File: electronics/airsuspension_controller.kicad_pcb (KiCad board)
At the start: 2 copper layers, 100 x 100 mm, 113 parts, among them Q1 BSS138, Q2 BC847, U1 ITS5215L, U10 Teensy3.1, U2 BTS6133D, U3 ITS5215L, U4 ITS5215L, U5 ITS5215L, U6 LM224, U7 LM224, U8 SN65HVD1050D, U9 LM2574M-5

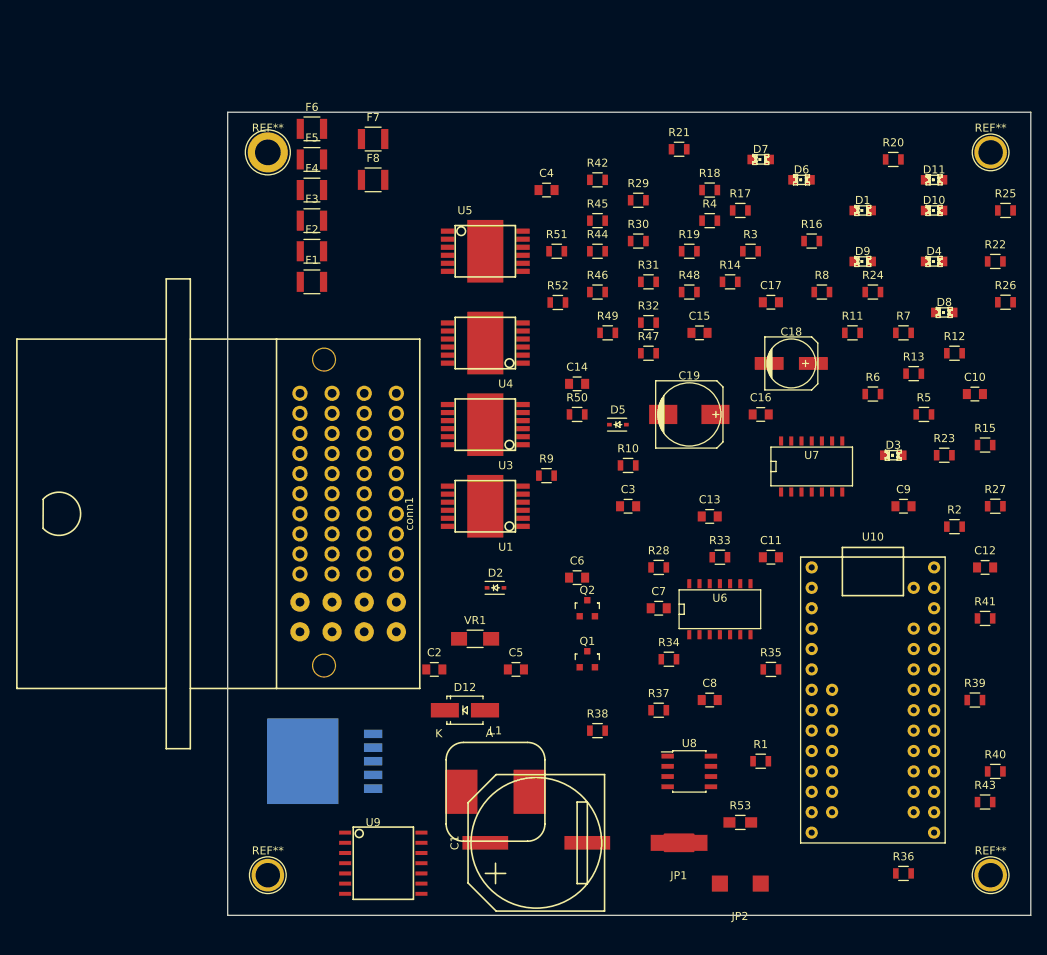
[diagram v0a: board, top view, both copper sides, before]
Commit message: Changed to a more stable powersupply (3Amps 5V and separate 3.3v) + some few cleanups due to updated kicad
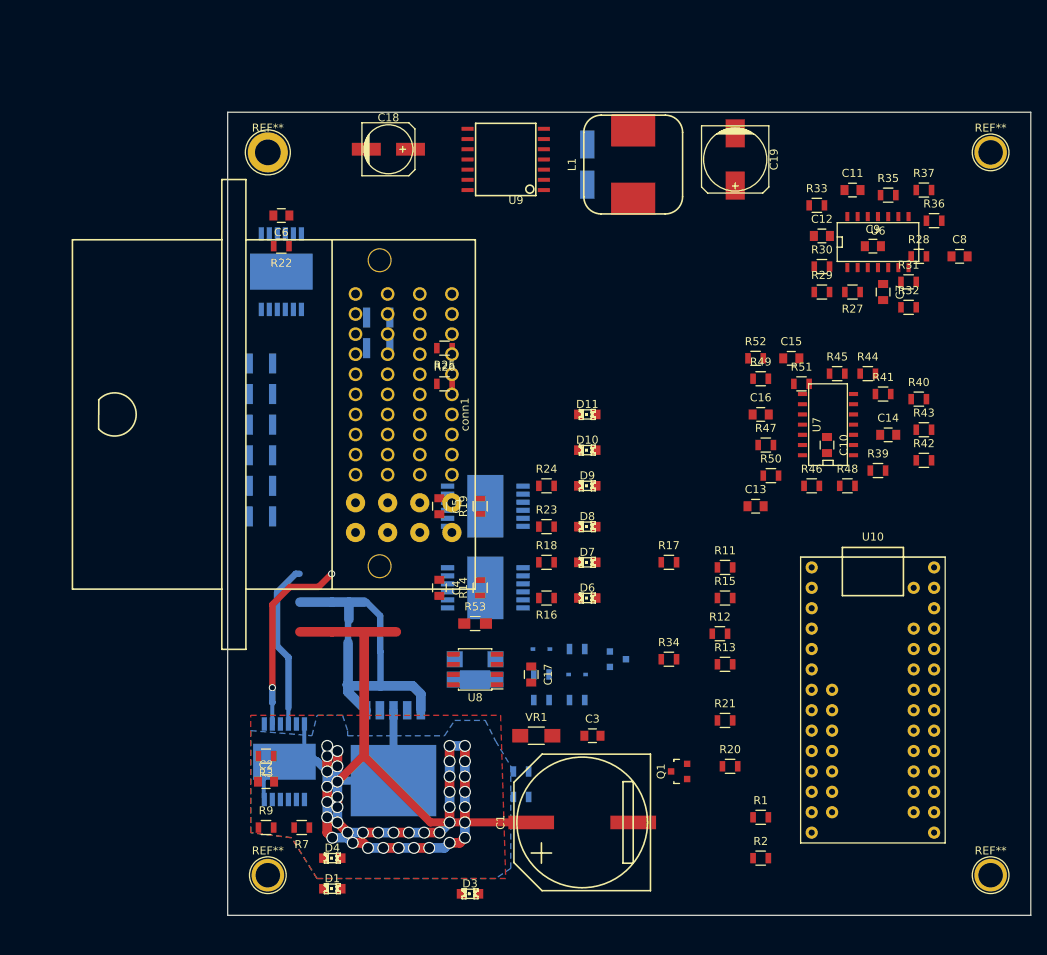
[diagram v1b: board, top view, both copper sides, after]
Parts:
- D12, D2, D5, F1, F2, F3, F4, F5, F6, F7, F8, JP1, JP2, Q2, R10, R38, R4, R5, R6, R8, U1, U3, U4, U5: moved to B.Cu
- moved D1 107.2 mm to (113.0, 146.7)
- moved D4 105.5 mm to (113.0, 142.9)
- moved R7 97.0 mm to (109.2, 139.1), turned to 180 degrees
- moved U9 88.9 mm to (134.6, 55.9), turned to 180 degrees
- moved R22 88.9 mm to (106.7, 66.7), turned to 180 degrees
- moved R3 87.1 mm to (104.8, 130.2), turned to 180 degrees
- moved R36 81.4 mm to (188.0, 63.5)
- moved L1 80.0 mm to (150.5, 56.5), turned to 90 degrees
- moved R20 78.2 mm to (162.6, 131.4)
- moved D3 75.9 mm to (130.2, 147.3)
- moved R37 72.7 mm to (186.7, 59.7)
- moved R4 72.5 mm to (136.5, 132.1)
- moved R25 71.9 mm to (127.0, 79.4), turned to 180 degrees
- moved R21 71.3 mm to (161.9, 125.7)
- moved R26 70.6 mm to (127.0, 83.8)
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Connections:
- C11 pad 2: GND -> Net-(C11-Pad2)
- C12 pad 2: GND -> Net-(C12-Pad2)
- conn1 pad L1: GNDPWR -> /Outputs/Compressor_OUT
- conn1 pad L4: /Outputs/Compressor_OUT -> GNDPWR
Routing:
- net +12V_bat: track 0.00 -> 168.8 mm, vias 0 -> 40
- net /Outputs/Compressor_OUT: track 0.00 -> 46.0 mm
- net /Outputs/RightFill_OUT: track 0.00 -> 23.9 mm, vias 0 -> 2
- net /Outputs/LeftFill_Out: track 0.00 -> 20.8 mm
- added copper zone on B.Cu, net +12V_bat
- added copper zone on F.Cu, net +12V_bat
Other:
- net class power: clearance 0.45 -> 0.376

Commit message: First placement with a ModICE enclosure
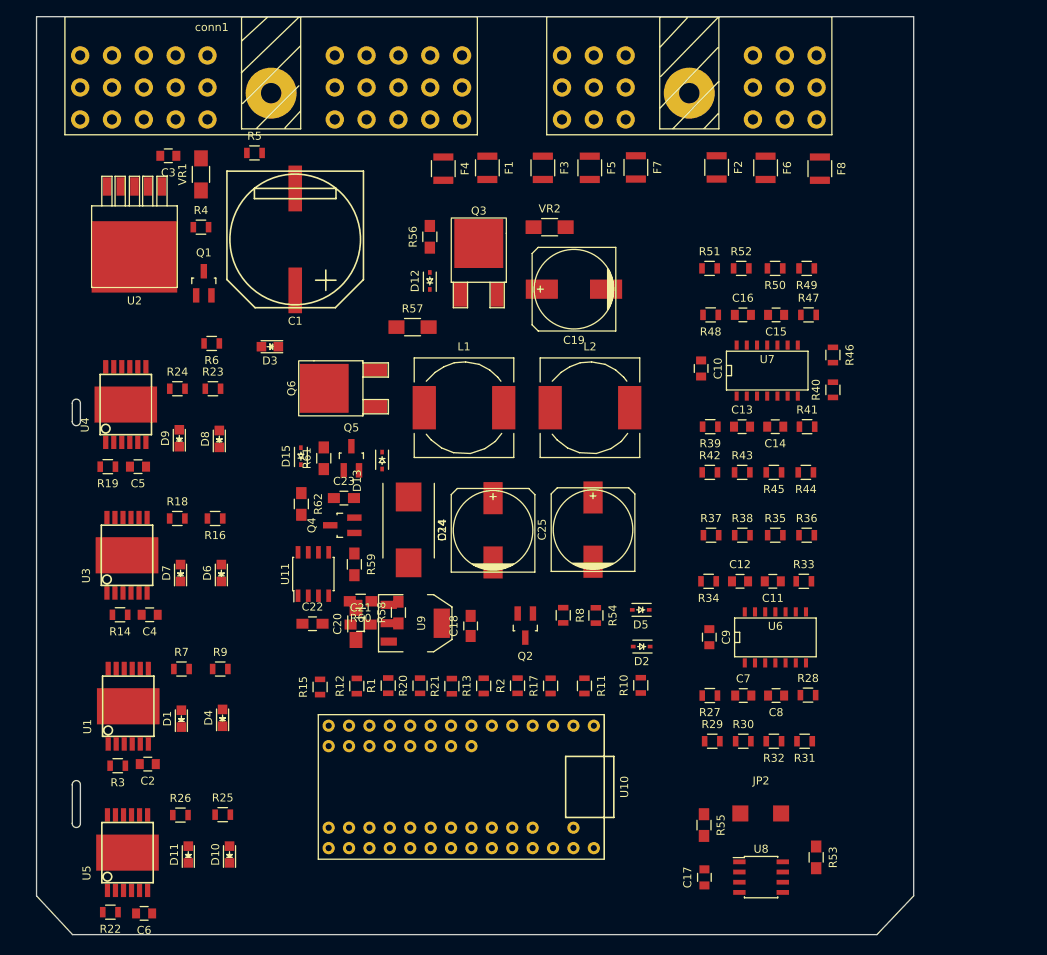
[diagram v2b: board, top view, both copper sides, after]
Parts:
- removed JP1: CAN_fullspeed, Oddities:NetTie-I_Connected_SMD
- removed REF** (x4): 1pin, Connect:1pin
- added C20: 10uF, Capacitors_SMD:C_1206_HandSoldering, F.Cu at (116.0, 113.7)
- added C21: 100n, Capacitors_SMD:C_0805_HandSoldering, F.Cu at (116.6, 113.8)
- added C22: 1n, Capacitors_SMD:C_0805_HandSoldering, F.Cu at (110.6, 113.7)
- added C23: 100n, Capacitors_SMD:C_0805_HandSoldering, F.Cu at (114.5, 98.0)
- added C24: 680uF, Capacitors_SMD:c_elec_10x10.5, F.Cu at (133.0, 102.1)
- added C25: 680uF, Capacitors_SMD:c_elec_10x10.5, F.Cu at (145.5, 102.0)
- added D13: 1n4148w, Diodes_SMD:SOD-323, F.Cu at (119.2, 93.4)
- added D14: schotky, Diodes_SMD:DO-214AB_Handsoldering, F.Cu at (122.5, 102.0)
- added D15: 1n4148w, Diodes_SMD:SOD-323, F.Cu at (109.1, 92.8)
- added L2: SRR1240-180M 17.4uH, Inductors_NEOSID:Neosid_Inductor_SM-NE127, F.Cu at (145.1, 86.8)
- added Q3: IPD50P04P4L-11, TO_SOT_Packages_SMD:TO-252-2Lead, F.Cu at (131.3, 72.7)
- added Q4: BC856, TO_SOT_Packages_SMD:SOT-23_Handsoldering, F.Cu at (114.3, 101.4)
- added Q5: BC856, TO_SOT_Packages_SMD:SOT-23_Handsoldering, F.Cu at (115.4, 93.1)
- added Q6: IPD060N03L G, TO_SOT_Packages_SMD:TO-252-2Lead, F.Cu at (118.4, 84.4)
- added R54: 1k, Resistors_SMD:R_0805, F.Cu at (145.8, 112.7)
- added R55: 10k, Resistors_SMD:R_0805_HandSoldering, F.Cu at (159.3, 138.8)
- added R56: 10k, Resistors_SMD:R_0805_HandSoldering, F.Cu at (125.2, 65.5)
- added R57: 0.031, Resistors_SMD:R_1206_HandSoldering, F.Cu at (123.0, 76.8)
- added R58: 1.2k, Resistors_SMD:R_0805_HandSoldering, F.Cu at (121.3, 112.3)
- added R59: 10k, Resistors_SMD:R_0805_HandSoldering, F.Cu at (115.8, 106.3)
- added R60: 3.6k, Resistors_SMD:R_0805_HandSoldering, F.Cu at (116.6, 110.9)
- added R61: 10k, Resistors_SMD:R_0805_HandSoldering, F.Cu at (112.0, 93.1)
- added R62: 10, Resistors_SMD:R_0805_HandSoldering, F.Cu at (109.2, 98.8)
- added U11: MC34063, Housings_SOIC:SOIC-8_3.9x4.9mm_Pitch1.27mm, F.Cu at (110.7, 107.5)
- added VR2: VR, Resistors_SMD:R_1206_HandSoldering, F.Cu at (140.1, 64.3)
- C18: value 47uF lowESR -> 100nF; footprint Capacitors_SMD:c_elec_6.3x7.7 -> Capacitors_SMD:C_0805_HandSoldering
- C19: value 470uF low esr -> 680uF; footprint Capacitors_SMD:c_elec_8x10.5 -> Capacitors_SMD:c_elec_10x10.5
- D1, D10, D11, D3, D4, D6, D7, D8, D9: footprint LEDs:LED-0805 -> LEDs:LED_0805
- D12: value SS110 -> 10v; footprint Diodes_SMD:Diode-SMA_Handsoldering -> Diodes_SMD:SOD-323; moved to F.Cu
- D2, D5, F1, F2, F3, F4, F5, F6, F7, F8, JP2, R10, R38, R4, R5, R6, U1, U3, U4, U5: moved to F.Cu
- L1: value 470uH -> SRR1240-180M 17.4uH; footprint kicad_lib:Inductor_MSS1260 -> Inductors_NEOSID:Neosid_Inductor_SM-NE127
- Q1: footprint Housings_SOT-23_SOT-143_TSOT-6:SOT-23 -> TO_SOT_Packages_SMD:SOT-23_Handsoldering
- Q2: footprint Housings_SOT-23_SOT-143_TSOT-6:SOT-23 -> TO_SOT_Packages_SMD:SOT-23_Handsoldering; moved to F.Cu
- R8: value 10k -> 1k; moved to F.Cu
- U2: footprint SMD_Packages:DPAK-5 -> kicad_lib:bts6133d; moved to F.Cu
- U9: value LM2574M-5 -> LD1117S33CTR; footprint kicad_lib:SOIC14_W -> TO_SOT_Packages_SMD:SOT-223
- conn1: value conn_molex_36638-48pin -> Conn48pin; footprint kicad_lib:Molex_48way_36638 -> cinch:Conn48pin
- moved C3 89.5 mm to (92.6, 55.4), turned to 180 degrees
- moved C6 88.6 mm to (89.6, 149.8)
- moved R22 85.6 mm to (85.4, 149.6)
- moved Q1 84.8 mm to (97.0, 71.3), turned to 0 degrees
- moved VR1 81.4 mm to (96.7, 57.7), turned to 90 degrees
- moved C1 80.9 mm to (108.4, 65.8), turned to 0 degrees
- moved R4 78.6 mm to (96.7, 64.3)
- moved R5 76.9 mm to (103.3, 55.1)
- moved U5 74.8 mm to (87.5, 142.2), turned to 90 degrees
- moved D11 74.0 mm to (95.1, 142.4), turned to 90 degrees
- moved U2 72.8 mm to (88.4, 59.2), turned to 180 degrees
- moved D3 72.5 mm to (105.3, 79.2), turned to 180 degrees
- moved F2 69.2 mm to (160.9, 56.9), turned to 270 degrees
- moved R6 68.4 mm to (98.0, 78.8)
- moved D10 67.2 mm to (100.2, 142.4), turned to 90 degrees
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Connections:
- net /CAN_bus/CAN_RX renamed /CAN_RX
- net /CAN_bus/CAN_TX renamed /CAN_TX
- net /Inputs/AnalogSpare_3.3V renamed /AnalogSpare_3.3V
- net /Inputs/LeftHeightPot_3.3V renamed /LeftHeight_3.3V
- net /Inputs/LeftPressure_3.3V renamed /LeftPressure_3.3V
- net /Inputs/RightHeightPot_3.3V renamed /RightHeight_3.3V
- net /Inputs/RightPressure_3.3V renamed /RightPressure_3.3V
- net /Inputs/SpareTemp_3.3V renamed /SpareTemp_3.3V
- net /Microcontroller/Airdryer_DIAG renamed /Airdryer_DIAG
- net /Microcontroller/Airdryer_ON renamed /Airdryer_ON
- net /Microcontroller/CompressorTemp_3.3V renamed /CompressorTemp_3.3V
- net /Microcontroller/Compressor_DIAG renamed /Compressor_DIAG
- net /Microcontroller/Compressor_ON renamed /Compressor_ON
- net /Microcontroller/Compressor_Pressure_3.3V renamed /CompressorPressure_3.3V
- net /Microcontroller/LeftDump_DIAG renamed /LeftDump_DIAG
- net /Microcontroller/LeftDump_ON renamed /LeftDump_ON
- net /Microcontroller/LeftFill_DIAG renamed /LeftFill_DIAG
- net /Microcontroller/LeftFill_ON renamed /LeftFill_ON
- net /Microcontroller/LeftSuck_DIAG renamed /LeftSuck_DIAG
- net /Microcontroller/LeftSuck_ON renamed /LeftSuck_ON
- net /Microcontroller/RightDump_DIAG renamed /RightDump_DIAG
- net /Microcontroller/RightDump_ON renamed /RightDump_ON
- net /Microcontroller/RightFill_DIAG renamed /RightFill_DIAG
- net /Microcontroller/RightFill_ON renamed /RightFill_ON
- net /Microcontroller/RightSuck_DIAG renamed /RightSuck_DIAG
- net /Microcontroller/RightSuck_ON renamed /RightSuck_ON
- net /Microcontroller/Spare1_Diag renamed /Spare1_DIAG
- net /Microcontroller/Spare1_ON renamed /Spare1_ON
- C11 pad 2: Net-(C11-Pad2) -> GND
- C12 pad 2: Net-(C12-Pad2) -> GND
- C18 pad 1: /5V power/+12V_IGN -> +5V
- C19 pad 1: +5V -> /5V power/+12V_IGN_SAFE
- D1 pad 1: Net-(D1-Pad1) -> GNDPWR
- D1 pad 2: GNDPWR -> Net-(D1-Pad2)
- D10 pad 1: Net-(D10-Pad1) -> GNDPWR
- D10 pad 2: GNDPWR -> Net-(D10-Pad2)
- D11 pad 1: Net-(D11-Pad1) -> GNDPWR
- D11 pad 2: GNDPWR -> Net-(D11-Pad2)
- D12 pad 1: GND -> /5V power/+12V_IGN_SAFE
- D3 pad 1: Net-(D3-Pad1) -> GNDPWR
- D3 pad 2: GNDPWR -> Net-(D3-Pad2)
- D4 pad 1: Net-(D4-Pad1) -> GNDPWR
- D4 pad 2: GNDPWR -> Net-(D4-Pad2)
- D5 pad 1: GND -> /CompressorCurrent_3.3V
- D5 pad 2: /Microcontroller/Compressor_Current -> GND
- D6 pad 1: Net-(D6-Pad1) -> GNDPWR
- D6 pad 2: GNDPWR -> Net-(D6-Pad2)
- D7 pad 1: Net-(D7-Pad1) -> GNDPWR
- D7 pad 2: GNDPWR -> Net-(D7-Pad2)
- D8 pad 1: Net-(D8-Pad1) -> GNDPWR
- D8 pad 2: GNDPWR -> Net-(D8-Pad2)
- D9 pad 1: Net-(D9-Pad1) -> GNDPWR
- D9 pad 2: GNDPWR -> Net-(D9-Pad2)
- F1 pad 1: /Inputs/CompressorPressure_5V -> /CompressorPressure_5V
- F2 pad 1: /Inputs/RightHeightPot_5V -> /RightHeightPot_5V
- F3 pad 1: /Inputs/LeftPressure_5V -> /LeftPressure_5V
- F4 pad 1: /Inputs/AnalogSpare_5V -> /AnalogSpare_5V
- F5 pad 1: /Inputs/RightPressure_5V -> /RightPressure_5V
- F6 pad 1: /Inputs/CompressorTemp_5V -> /CompressorTemp_5V
- F7 pad 1: /Inputs/LeftHeightPot_5V -> /LeftHeightPot_5V
- F8 pad 1: /Inputs/SpareTemp_5V -> /SpareTemp_5V
- L1 pad 1: Net-(D12-Pad2) -> Net-(C23-Pad2)
- L1 pad 2: +5V -> Net-(C24-Pad1)
- R10 pad 1: /Microcontroller/Compressor_Current -> /CompressorCurrent_3.3V
- R10 pad 2: Net-(D2-Pad2) -> Net-(D2-Pad1)
- R16 pad 1: Net-(D6-Pad1) -> Net-(D6-Pad2)
- R16 pad 2: /Outputs/RightDump_OUT -> /RightDump_OUT
- R18 pad 1: /Outputs/LeftDump_Out -> /LeftDump_OUT
- R18 pad 2: Net-(D7-Pad1) -> Net-(D7-Pad2)
- R23 pad 1: Net-(D8-Pad1) -> Net-(D8-Pad2)
- R23 pad 2: /Outputs/Spare1_OUT -> /Spare1_OUT
- R24 pad 1: /Outputs/Airdryer_Out -> /AirDryer_OUT
- R24 pad 2: Net-(D9-Pad1) -> Net-(D9-Pad2)
- R25 pad 1: Net-(D10-Pad1) -> Net-(D10-Pad2)
- R25 pad 2: /Outputs/RightSuck_OUT -> /RightSuck_OUT
- R26 pad 1: /Outputs/LeftSuck_Out -> /LeftSuck_OUT
- R26 pad 2: Net-(D11-Pad1) -> Net-(D11-Pad2)
- R27 pad 2: /Inputs/CompressorPressure_IN -> /CompressorPressure_IN
- R28 pad 2: /Inputs/RightHeightPot_IN -> /RightHeightPot_IN
- R33 pad 2: /Inputs/LeftPressure_IN -> /LeftPressure_IN
- R34 pad 2: /Inputs/AnalogSpare_IN -> /AnalogSpare_IN
- R39 pad 2: /Inputs/RightPressure_IN -> /RightPressure_IN
- R40 pad 1: /Inputs/CompressorTemp_IN -> /CompressorTemp_IN
- R41 pad 2: /Inputs/CompressorTemp_IN -> /CompressorTemp_IN
- R46 pad 1: /Inputs/SpareTemp_IN -> /SpareTemp_IN
- R47 pad 2: /Inputs/LeftHeightPot_IN -> /LeftHeightPot_IN
- R48 pad 2: /Inputs/SpareTemp_IN -> /SpareTemp_IN
- R5 pad 1: Net-(D2-Pad2) -> Net-(D2-Pad1)
- R53 pad 1: /CAN_bus/CAN_HI -> /CAN_HI
- R53 pad 2: /CAN_bus/CAN_LO -> /CAN_LO
- R6 pad 1: Net-(D3-Pad1) -> Net-(D3-Pad2)
- R6 pad 2: /Outputs/Compressor_OUT -> /Compressor_OUT
- R7 pad 1: Net-(D1-Pad1) -> Net-(D1-Pad2)
- R7 pad 2: /Outputs/RightFill_OUT -> /RightFill_OUT
- R8 pad 2: Net-(D2-Pad1) -> Net-(D2-Pad2)
- R9 pad 1: /Outputs/LeftFill_Out -> /LeftFill_OUT
- R9 pad 2: Net-(D4-Pad1) -> Net-(D4-Pad2)
- U1 pad 10: /Outputs/LeftFill_Out -> /LeftFill_OUT
- U1 pad 8: /Outputs/RightFill_OUT -> /RightFill_OUT
- U10 pad 28: /Microcontroller/Compressor_Current -> /CompressorCurrent_3.3V
- U10 pad 30: +3.3V -> Net-(U10-Pad30)
- U2 pad 1: /Outputs/Compressor_OUT -> /Compressor_OUT
- U2 pad 4: Net-(D2-Pad2) -> Net-(D2-Pad1)
- U2 pad 5: /Outputs/Compressor_OUT -> /Compressor_OUT
- U3 pad 10: /Outputs/LeftDump_Out -> /LeftDump_OUT
- U3 pad 8: /Outputs/RightDump_OUT -> /RightDump_OUT
- U4 pad 10: /Outputs/Airdryer_Out -> /AirDryer_OUT
- U4 pad 8: /Outputs/Spare1_OUT -> /Spare1_OUT
- U5 pad 10: /Outputs/LeftSuck_Out -> /LeftSuck_OUT
- U5 pad 8: /Outputs/RightSuck_OUT -> /RightSuck_OUT
- U8 pad 6: /CAN_bus/CAN_LO -> /CAN_LO
- U8 pad 7: /CAN_bus/CAN_HI -> /CAN_HI
- U9 pad 2: GND -> +3.3V
- U9 pad 4: GND -> (no net)
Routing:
- net +12V_bat: track 168.8 -> 0.00 mm, vias 40 -> 0
- net /Outputs/Compressor_OUT: track 46.0 -> 0.00 mm
- net /Outputs/RightFill_OUT: track 23.9 -> 0.00 mm, vias 2 -> 0
- net /Outputs/LeftFill_Out: track 20.8 -> 0.00 mm
- removed copper zone on B.Cu, net +12V_bat
- removed copper zone on F.Cu, net +12V_bat
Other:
- board size 100 x 100 mm -> 109.2 x 114.3 mm
- net class Default: clearance 0.254 -> 0.2; trace_width 0.4 -> 0.25; via_dia 0.889 -> 0.6; via_drill 0.635 -> 0.4
- net class outputs removed
- net class power removed
- net class signal removed
- rule pad_to_mask_clearance: 0 -> 0.2
- rule trace_clearance: 0.254 -> 0.2
- rule trace_min: 0.254 -> 0.2
- rule via_min_drill: 0.508 -> 0.3
- rule via_min_size: 0.889 -> 0.4
- board text added: "Zone 2 max 0.600" (15,24mm) height over pcb"
- board text added: "Zone 4 height increases from zone3 to zone1"
- board text added: "Zone1 max 1.140" (28.96mm) height over board"
- board text added: "Zone3 Max 0.900" (22.86mm) height over pcb"

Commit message: PCB routing done
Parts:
- added REF**: github.com/mumme74, Symbols:Symbol_OSHW-Logo_SilkScreen, F.Cu at (107.6, 146.7)
- moved Q1 22.2 mm to (119.0, 68.1), turned to 180 degrees
- moved VR2 19.2 mm to (121.6, 59.2), turned to 90 degrees
- moved R4 18.7 mm to (113.1, 55.5)
- moved R46 15.4 mm to (160.1, 78.2), turned to 0 degrees
- moved D3 12.1 mm to (93.7, 75.7)
- moved C3 11.5 mm to (97.0, 66.0), turned to 270 degrees
- moved R55 10.8 mm to (169.7, 135.9), turned to 0 degrees
- moved R6 9.82 mm to (88.6, 75.8)
- moved R56 9.45 mm to (120.1, 73.5), turned to 180 degrees
- moved R62 8.90 mm to (116.2, 104.3)
- moved U8 8.54 mm to (162.6, 137.6)
- moved C17 8.36 mm to (155.9, 137.7)
- moved R59 8.19 mm to (109.4, 101.1), turned to 180 degrees
- moved C20 7.72 mm to (123.7, 113.8)
- moved C18 7.52 mm to (137.8, 114.0)
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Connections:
- Q1 pad 2: GND -> GNDPWR
- conn1 pad 19: /Compressor_OUT -> +12V_bat
- conn1 pad 20: /Compressor_OUT -> +12V_bat
- conn1 pad 21: /Compressor_OUT -> +12V_bat
- conn1 pad 22: /Compressor_OUT -> +12V_bat
- conn1 pad 24: +12V_bat -> /Compressor_OUT
- conn1 pad 25: +12V_bat -> /Compressor_OUT
- conn1 pad 26: +12V_bat -> /Compressor_OUT
- conn1 pad 27: +12V_bat -> /Compressor_OUT
- conn1 pad 30: /AirDryer_OUT -> GNDPWR
- conn1 pad 31: GNDPWR -> /AirDryer_OUT
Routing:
- net GND: track 0.00 -> 638.7 mm, vias 0 -> 12
- net +12V_bat: track 0.00 -> 401.7 mm
- net +5V: track 0.00 -> 280.5 mm, vias 0 -> 7
- net GNDPWR: track 0.00 -> 280.0 mm
- net Net-(D2-Pad1): track 0.00 -> 150.4 mm, vias 0 -> 4
- net /RightSuck_OUT: track 0.00 -> 142.8 mm, vias 0 -> 2
- net /Spare1_ON: track 0.00 -> 116.8 mm, vias 0 -> 1
- net /CAN_LO: track 0.00 -> 113.2 mm
- net /LeftSuck_OUT: track 0.00 -> 113.0 mm, vias 0 -> 2
- net /CAN_HI: track 0.00 -> 112.0 mm
- net /Spare1_DIAG: track 0.00 -> 104.4 mm, vias 0 -> 2
- net /Compressor_OUT: track 0.00 -> 103.4 mm, vias 0 -> 2
- net /RightFill_OUT: track 0.00 -> 102.6 mm, vias 0 -> 2
- net /SpareTemp_3.3V: track 0.00 -> 102.6 mm, vias 0 -> 1
- net /LeftFill_OUT: track 0.00 -> 100.5 mm, vias 0 -> 2
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- added copper zone on F.Cu, net +12V_bat
- added copper zone on B.Cu, net /+12V_IGN
- added copper zone on F.Cu, net /+12V_IGN
- added copper zone on B.Cu, net Net-(C24-Pad1)
- added copper zone on F.Cu, net Net-(C24-Pad1)
- added copper zone on B.Cu, net Net-(D15-Pad2)
- added copper zone on F.Cu, net Net-(D15-Pad2)
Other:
- board text added: "Attention! Cut the USB power bridge on Teensy 3.1"
- board text added: "Bridge JP2 for silent mode (never send on CAN)"
- board text added: "R53 only on endnode"
- board text added: "airsuspension controller (rev 1, 2016-04)"
